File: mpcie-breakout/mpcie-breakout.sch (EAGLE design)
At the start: 34 parts, among them K1 694108106102, U1 IP4234CZ6, U2 LD1085D2T33R, X1 MPCIE-JAE, X2 MINI-USB-SHIELD-UX60-MB-5ST

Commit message: mpcie-breakout: Add Digikey LINK for all major parts
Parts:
- C1, C2, C4: CLASS (none) -> CAPACITOR; DESCRIPTION (none) -> NO DESCRIPTION; LINK (none) -> UNKNOWN LINK; MANUFACTURER (none) -> UNKNOWN MANUFACTURER; MANUFACTURERPARTNUMBER (none) -> UNKNOWN MANUFACTURER PART NUMBER; POPULATED (none) -> TRUE; ROHSCERTIFICATE (none) -> UNKNOWN ROHS CERTIFICATE; SOURCE (none) -> UNKNOWN SOURCE; SOURCEPARTNUMBER (none) -> UNKNOWN SOURCE PART NUMBER
- C3: CLASS (none) -> CAPACITOR; DESCRIPTION (none) -> NO DESCRIPTION; LINK (none) -> http://www.digikey.com/product-detail/en/nichicon/UUR0J471M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; MANUFACTURER (none) -> UNKNOWN MANUFACTURER; MANUFACTURERPARTNUMBER (none) -> UNKNOWN MANUFACTURER PART NUMBER; POPULATED (none) -> TRUE; ROHSCERTIFICATE (none) -> UNKNOWN ROHS CERTIFICATE; SOURCE (none) -> UNKNOWN SOURCE; SOURCEPARTNUMBER (none) -> UNKNOWN SOURCE PART NUMBER
- JP1, JP2, JP3, JP4: CLASS (none) -> CONNECTOR\JUMPER; DESCRIPTION (none) -> NO DESCRIPTION; LINK (none) -> UNKNOWN LINK; MANUFACTURER (none) -> UNKNOWN MANUFACTURER; MANUFACTURERPARTNUMBER (none) -> UNKNOWN MANUFACTURER PART NUMBER; POPULATED (none) -> TRUE; ROHSCERTIFICATE (none) -> UNKNOWN ROHS CERTIFICATE; SOURCE (none) -> UNKNOWN SOURCE; SOURCEPARTNUMBER (none) -> UNKNOWN SOURCE PART NUMBER
- K1: CLASS (none) -> RELAY; DESCRIPTION (none) -> NO DESCRIPTION; LINK (none) -> http://www.digikey.com/product-detail/en/wurth-electronics-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; MANUFACTURER (none) -> UNKNOWN MANUFACTURER; MANUFACTURERPARTNUMBER (none) -> UNKNOWN MANUFACTURER PART NUMBER; POPULATED (none) -> TRUE; ROHSCERTIFICATE (none) -> UNKNOWN ROHS CERTIFICATE; SOURCE (none) -> UNKNOWN SOURCE; SOURCEPARTNUMBER (none) -> UNKNOWN SOURCE PART NUMBER
- LED1, LED2: CLASS (none) -> LED; DESCRIPTION (none) -> NO DESCRIPTION; LINK (none) -> UNKNOWN LINK; MANUFACTURER (none) -> UNKNOWN MANUFACTURER; MANUFACTURERPARTNUMBER (none) -> UNKNOWN MANUFACTURER PART NUMBER; POPULATED (none) -> TRUE; ROHSCERTIFICATE (none) -> UNKNOWN ROHS CERTIFICATE; SOURCE (none) -> UNKNOWN SOURCE; SOURCEPARTNUMBER (none) -> UNKNOWN SOURCE PART NUMBER
- R1, R2, R3, R4, R5: CLASS (none) -> RESISTOR; DESCRIPTION (none) -> NO DESCRIPTION; LINK (none) -> UNKNOWN LINK; MANUFACTURER (none) -> UNKNOWN MANUFACTURER; MANUFACTURERPARTNUMBER (none) -> UNKNOWN MANUFACTURER PART NUMBER; POPULATED (none) -> TRUE; ROHSCERTIFICATE (none) -> UNKNOWN ROHS CERTIFICATE; SOURCE (none) -> UNKNOWN SOURCE; SOURCEPARTNUMBER (none) -> UNKNOWN SOURCE PART NUMBER
- SIM1: CLASS (none) -> UNKNOWN CLASS; DESCRIPTION (none) -> NO DESCRIPTION; LINK (none) -> http://www.digikey.com/product-detail/en/jae-electronics/SF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; MANUFACTURER (none) -> UNKNOWN MANUFACTURER; MANUFACTURERPARTNUMBER (none) -> UNKNOWN MANUFACTURER PART NUMBER; POPULATED (none) -> TRUE; ROHSCERTIFICATE (none) -> UNKNOWN ROHS CERTIFICATE; SOURCE (none) -> UNKNOWN SOURCE; SOURCEPARTNUMBER (none) -> UNKNOWN SOURCE PART NUMBER
- U1: CLASS (none) -> IC; DESCRIPTION (none) -> NO DESCRIPTION; LINK (none) -> http://www.digikey.com/product-detail/en/nxp-semiconductors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; MANUFACTURER (none) -> UNKNOWN MANUFACTURER; MANUFACTURERPARTNUMBER (none) -> UNKNOWN MANUFACTURER PART NUMBER; POPULATED (none) -> TRUE; ROHSCERTIFICATE (none) -> UNKNOWN ROHS CERTIFICATE; SOURCE (none) -> UNKNOWN SOURCE; SOURCEPARTNUMBER (none) -> UNKNOWN SOURCE PART NUMBER
- U2: CLASS (none) -> IC; DESCRIPTION (none) -> NO DESCRIPTION; LINK (none) -> http://www.digikey.com/product-detail/en/stmicroelectronics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; MANUFACTURER (none) -> UNKNOWN MANUFACTURER; MANUFACTURERPARTNUMBER (none) -> UNKNOWN MANUFACTURER PART NUMBER; POPULATED (none) -> TRUE; ROHSCERTIFICATE (none) -> UNKNOWN ROHS CERTIFICATE; SOURCE (none) -> UNKNOWN SOURCE; SOURCEPARTNUMBER (none) -> UNKNOWN SOURCE PART NUMBER
- X1: CLASS (none) -> CONNECTOR; DESCRIPTION (none) -> NO DESCRIPTION; LINK (none) -> https://www.digikey.de/product-detail/de/jae-electronics/MM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; MANUFACTURER (none) -> UNKNOWN MANUFACTURER; MANUFACTURERPARTNUMBER (none) -> UNKNOWN MANUFACTURER PART NUMBER; POPULATED (none) -> TRUE; ROHSCERTIFICATE (none) -> UNKNOWN ROHS CERTIFICATE; SOURCE (none) -> UNKNOWN SOURCE; SOURCEPARTNUMBER (none) -> UNKNOWN SOURCE PART NUMBER
- X2: CLASS (none) -> CONNECTOR; DESCRIPTION (none) -> NO DESCRIPTION; LINK (none) -> http://www.digikey.com/product-detail/en/hirose-electric-co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; MANUFACTURER (none) -> UNKNOWN MANUFACTURER; MANUFACTURERPARTNUMBER (none) -> UNKNOWN MANUFACTURER PART NUMBER; POPULATED (none) -> TRUE; ROHSCERTIFICATE (none) -> UNKNOWN ROHS CERTIFICATE; SOURCE (none) -> UNKNOWN SOURCE; SOURCEPARTNUMBER (none) -> UNKNOWN SOURCE PART NUMBER

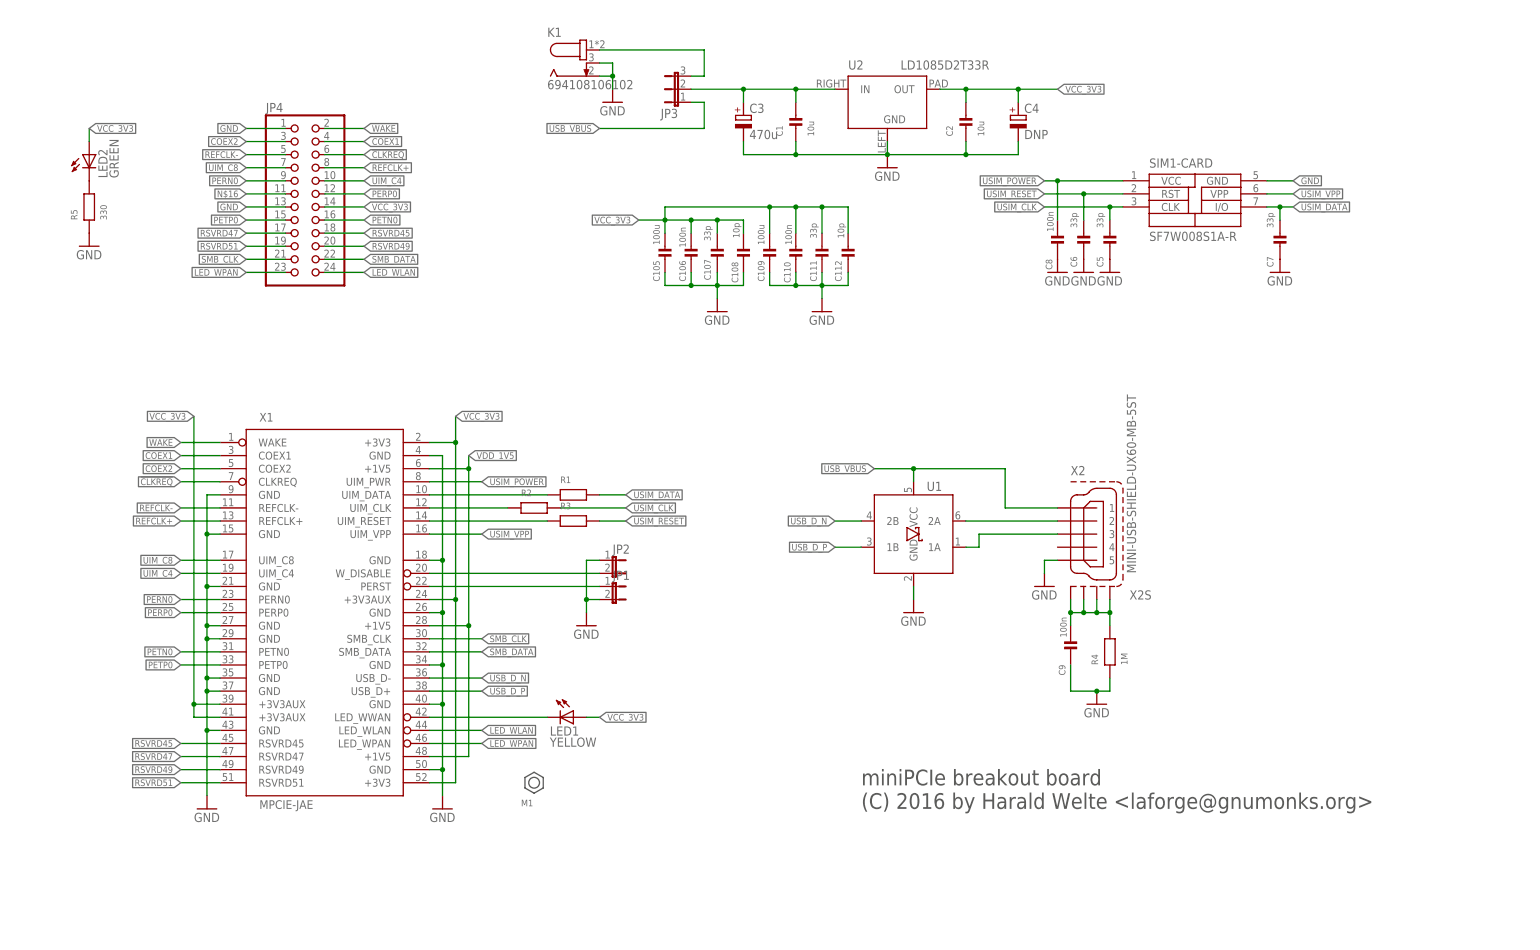
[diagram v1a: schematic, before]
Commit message: mpcie-breakout: Beautify schematics
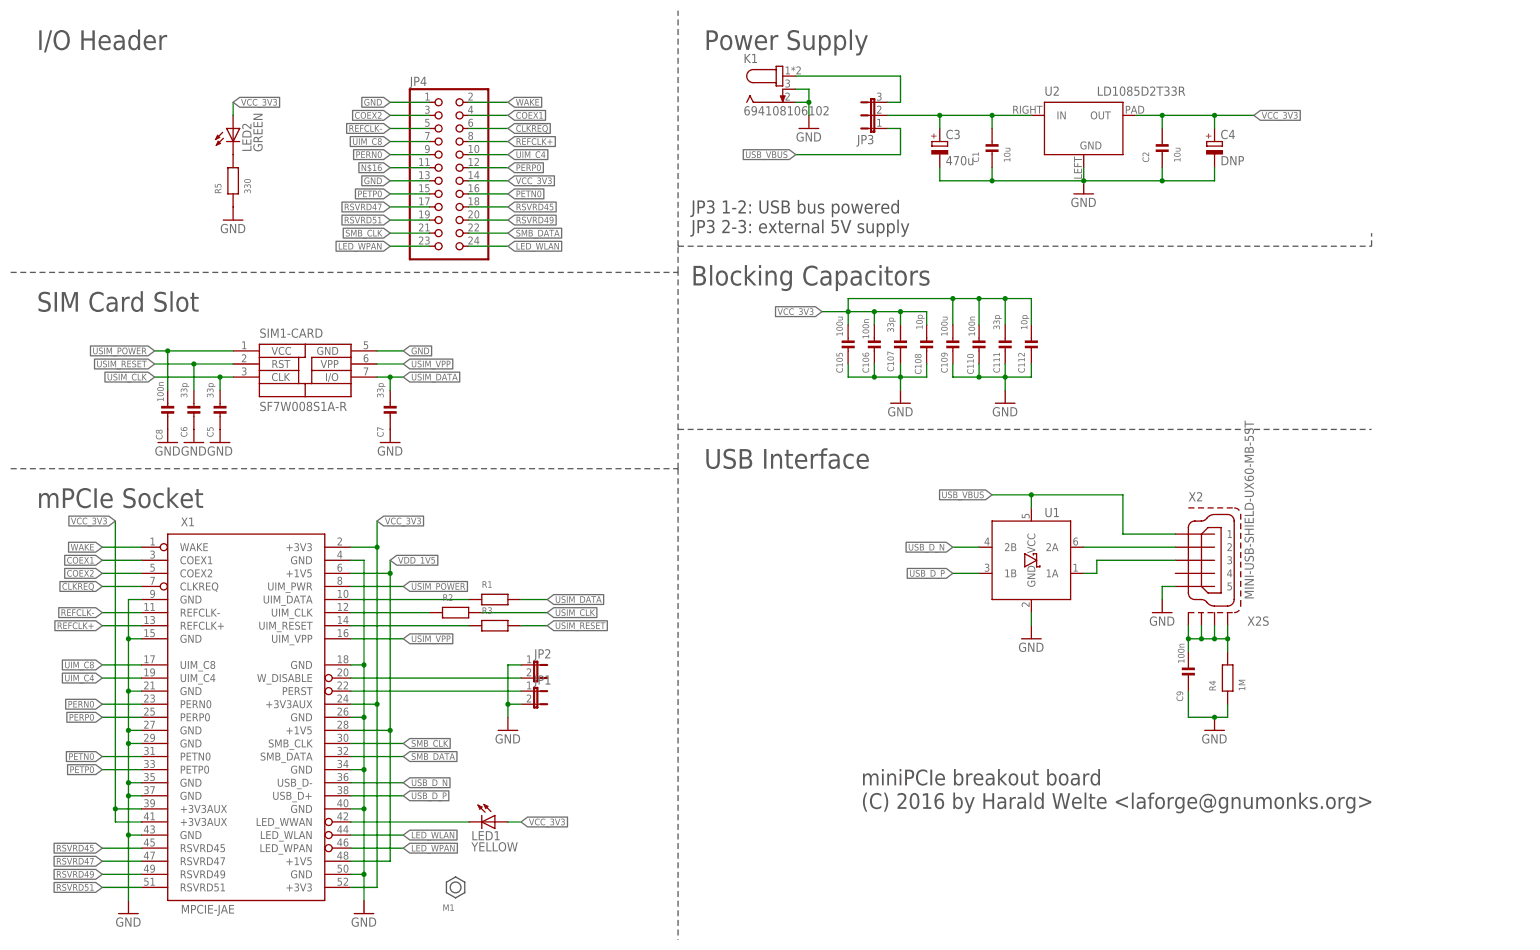
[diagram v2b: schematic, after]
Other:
- note added: "Blocking Capacitors"
- note added: "I/O Header"
- note added: "JP3 1-2: USB bus powered JP3 2-3: external 5V supply"
- note added: "Power Supply"
- note added: "SIM Card Slot"
- note added: "USB Interface"
- note added: "mPCIe Socket"
- moved on the sheet: C1, C105, C106, C107, C108, C109, C110, C111, C112, C2, C3, C4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

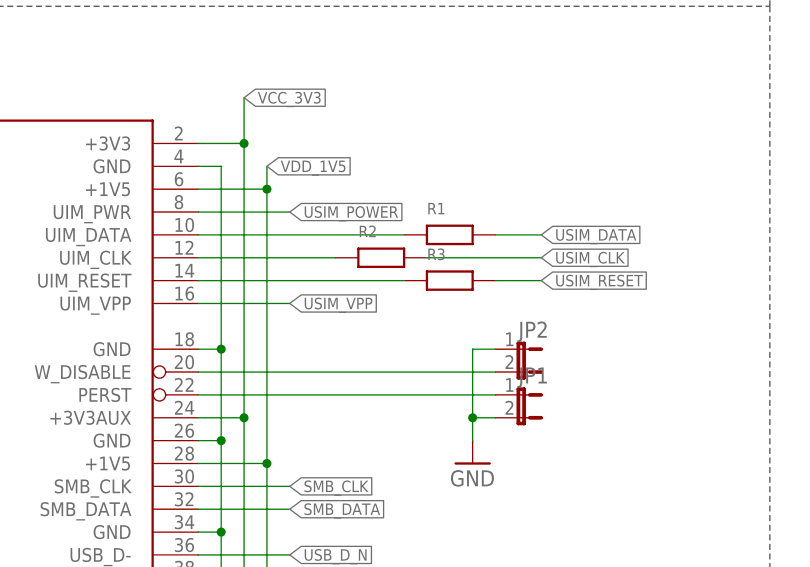
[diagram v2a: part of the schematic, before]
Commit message: mpci-breakout: Add BOM attributes + export BOM
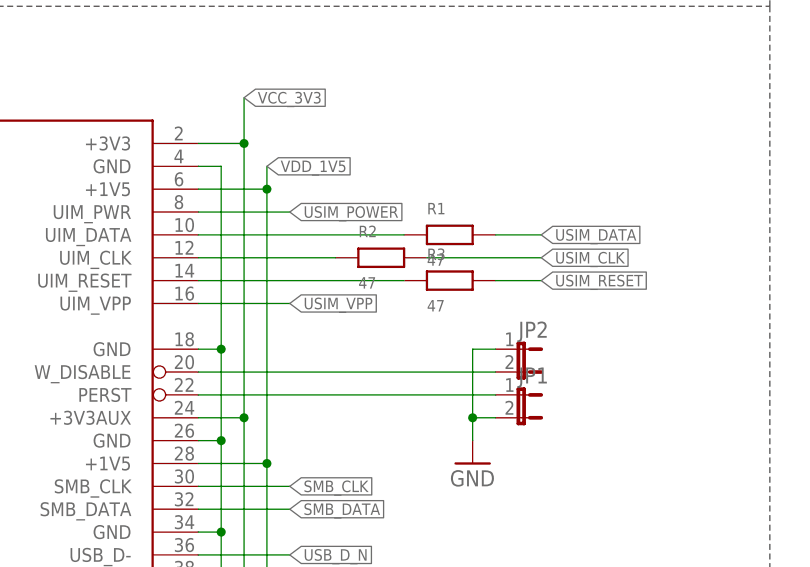
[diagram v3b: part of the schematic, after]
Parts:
- C1, C2: DESCRIPTION NO DESCRIPTION -> 10µF 16V Ceramic Capacitor X5R 0805 (2012 Metric) 0.079" L 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; LINK UNKNOWN LINK -> http://www.digikey.com/product-detail/en/samsung-electro-me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; MANUFACTURER UNKNOWN MANUFACTURER -> Samsung Electro-Mechanics America, Inc.; MANUFACTURERPARTNUMBER UNKNOWN MANUFACTURER PART NUMBER -> CL21A106KOQNNNG; SOURCE UNKNOWN SOURCE -> DIGIKEY; SOURCEPARTNUMBER UNKNOWN SOURCE PART NUMBER -> 1276-6455-1-ND
- C105, C109: LINK http://www.digikey.de/product-detail/de/CL32A107MQVNNNE/127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 -> http://www.digikey.com/product-detail/en/CL32A107MQVNNNE/12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
- C106, C110, C8, C9: LINK http://www.digikey.de/product-detail/de/foo/1276-1005-1-ND -> http://www.digikey.com/product-detail/en/foo/1276-1005-1-ND
- C107, C111, C5, C6, C7: LINK http://www.digikey.de/product-detail/de/CL05C330JB5NNNC/127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 -> http://www.digikey.com/product-detail/en/CL05C330JB5NNNC/12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
- C108, C112: LINK http://www.digikey.de/product-detail/de/C0603C100J5GACTU/39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 -> http://www.digikey.com/product-detail/en/C0603C100J5GACTU/3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
- C3: DESCRIPTION NO DESCRIPTION -> 470µF 6.3V Aluminum Capacitors Radial, Can - SMD 2000 Hrs @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; MANUFACTURER UNKNOWN MANUFACTURER -> Nichicon; MANUFACTURERPARTNUMBER UNKNOWN MANUFACTURER PART NUMBER -> UUR0J471MNL1GS; SOURCE UNKNOWN SOURCE -> DIGIKEY; SOURCEPARTNUMBER UNKNOWN SOURCE PART NUMBER -> 493-6207-1-ND
- JP4: DESCRIPTION NO DESCRIPTION -> 24 Positions Header, Unshrouded, Breakaway Connector 0.100"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; LINK UNKNOWN LINK -> http://www.digikey.com/product-detail/en/sullins-connector-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; MANUFACTURER UNKNOWN MANUFACTURER -> Sullins Connector Solutions; MANUFACTURERPARTNUMBER UNKNOWN MANUFACTURER PART NUMBER -> PRPC012DAAN-RC; SOURCE UNKNOWN SOURCE -> DIGIKEY; SOURCEPARTNUMBER UNKNOWN SOURCE PART NUMBER -> S2011EC-12-ND
- K1: DESCRIPTION NO DESCRIPTION -> Power Barrel Connector Jack 2.50mm ID (0.098"), 5.50mm OD (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; MANUFACTURER UNKNOWN MANUFACTURER -> Wurth Electronics Inc; MANUFACTURERPARTNUMBER UNKNOWN MANUFACTURER PART NUMBER -> 694108106102; SOURCE UNKNOWN SOURCE -> DIGIKEY; SOURCEPARTNUMBER UNKNOWN SOURCE PART NUMBER -> 732-5933-1-ND
- R1, R2, R3: value (none) -> 47; DESCRIPTION NO DESCRIPTION -> RES SMD 47 OHM 5% 1/10W 0603; LINK UNKNOWN LINK -> http://www.digikey.com/product-detail/en/yageo/RC0603JR-074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; MANUFACTURER UNKNOWN MANUFACTURER -> Yageo; MANUFACTURERPARTNUMBER UNKNOWN MANUFACTURER PART NUMBER -> RC0603JR-0747RL; SOURCE UNKNOWN SOURCE -> DIGIKEY; SOURCEPARTNUMBER UNKNOWN SOURCE PART NUMBER -> 311-47GRCT-ND
- R4: DESCRIPTION NO DESCRIPTION -> RES SMD 1M OHM 5% 1/20W 0201; LINK UNKNOWN LINK -> http://www.digikey.com/product-detail/en/samsung-electro-me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; MANUFACTURER UNKNOWN MANUFACTURER -> Samsung Electro-Mechanics America, Inc.; MANUFACTURERPARTNUMBER UNKNOWN MANUFACTURER PART NUMBER -> RC0603J105CS; SOURCE UNKNOWN SOURCE -> DIGIKEY; SOURCEPARTNUMBER UNKNOWN SOURCE PART NUMBER -> 1276-3856-1-ND
- R5: DESCRIPTION NO DESCRIPTION -> RES SMD 330 OHM 5% 1/10W 0603; LINK UNKNOWN LINK -> http://www.digikey.com/product-detail/en/yageo/RC0603JR-073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; MANUFACTURER UNKNOWN MANUFACTURER -> Yageo; MANUFACTURERPARTNUMBER UNKNOWN MANUFACTURER PART NUMBER -> RC0603JR-07330RL; SOURCE UNKNOWN SOURCE -> DIGIKEY; SOURCEPARTNUMBER UNKNOWN SOURCE PART NUMBER -> 311-330GRCT-ND
- SIM1: DESCRIPTION NO DESCRIPTION -> 8 (6 + 2) Position Card Connector SIM Card Surface Mount, R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; MANUFACTURER UNKNOWN MANUFACTURER -> JAE Electronics; MANUFACTURERPARTNUMBER UNKNOWN MANUFACTURER PART NUMBER -> SF7W008S1AE900; SOURCE UNKNOWN SOURCE -> DIGIKEY; SOURCEPARTNUMBER UNKNOWN SOURCE PART NUMBER -> 670-2337-1-ND
- U1: DESCRIPTION NO DESCRIPTION -> TVS DIODE 5.5VWM 6TSOP; MANUFACTURER UNKNOWN MANUFACTURER -> NXP Semiconductors; MANUFACTURERPARTNUMBER UNKNOWN MANUFACTURER PART NUMBER -> IP4234CZ6,125; SOURCE UNKNOWN SOURCE -> DIGIKEY; SOURCEPARTNUMBER UNKNOWN SOURCE PART NUMBER -> 568-5869-1-ND
- U2: DESCRIPTION NO DESCRIPTION -> Linear Voltage Regulator IC Positive Fixed 1 Output 3.3V 3A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; MANUFACTURER UNKNOWN MANUFACTURER -> STMicroelectronics; MANUFACTURERPARTNUMBER UNKNOWN MANUFACTURER PART NUMBER -> LD1085D2T33R; SOURCE UNKNOWN SOURCE -> DIGIKEY; SOURCEPARTNUMBER UNKNOWN SOURCE PART NUMBER -> 497-1222-1-ND
- X1: DESCRIPTION NO DESCRIPTION -> CONN MINI EXPRESS CARD 52POS SMD; LINK https://www.digikey.de/product-detail/de/jae-electronics/MM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 -> http://www.digikey.com/product-detail/en/jae-electronics/MM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; MANUFACTURER UNKNOWN MANUFACTURER -> JAE Electronics; MANUFACTURERPARTNUMBER UNKNOWN MANUFACTURER PART NUMBER -> MM60-52B1-E1-R650; SOURCE UNKNOWN SOURCE -> DIGIKEY; SOURCEPARTNUMBER UNKNOWN SOURCE PART NUMBER -> 670-2275-1-ND
- X2: DESCRIPTION NO DESCRIPTION -> USB - mini B USB 2.0 Receptacle Connector 5 Position Surfac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; MANUFACTURER UNKNOWN MANUFACTURER -> Hirose Electric Co Ltd; MANUFACTURERPARTNUMBER UNKNOWN MANUFACTURER PART NUMBER -> UX60-MB-5ST; SOURCE UNKNOWN SOURCE -> DIGIKEY; SOURCEPARTNUMBER UNKNOWN SOURCE PART NUMBER -> H2959CT-ND

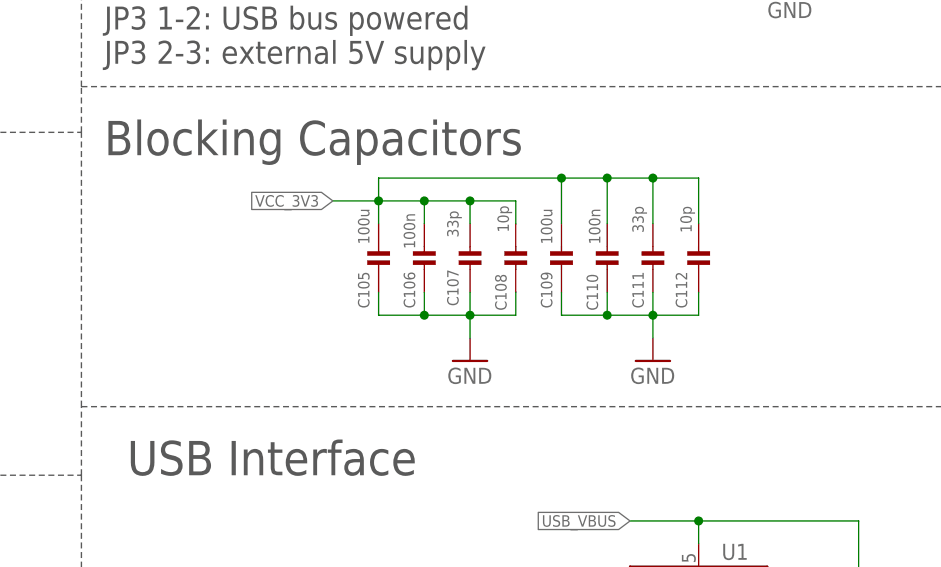
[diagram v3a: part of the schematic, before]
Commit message: mpcie-breakout: change 100uF caps from 1210 to 1206, reducing height
The current 100uF caps are too high at 2.9mm.  They touch the shielding
can of Quectel EC-20 modules, for exampel.  Let's use 1206 packaged
versions at 1.6mm instead.  Also, add two more, for safety.
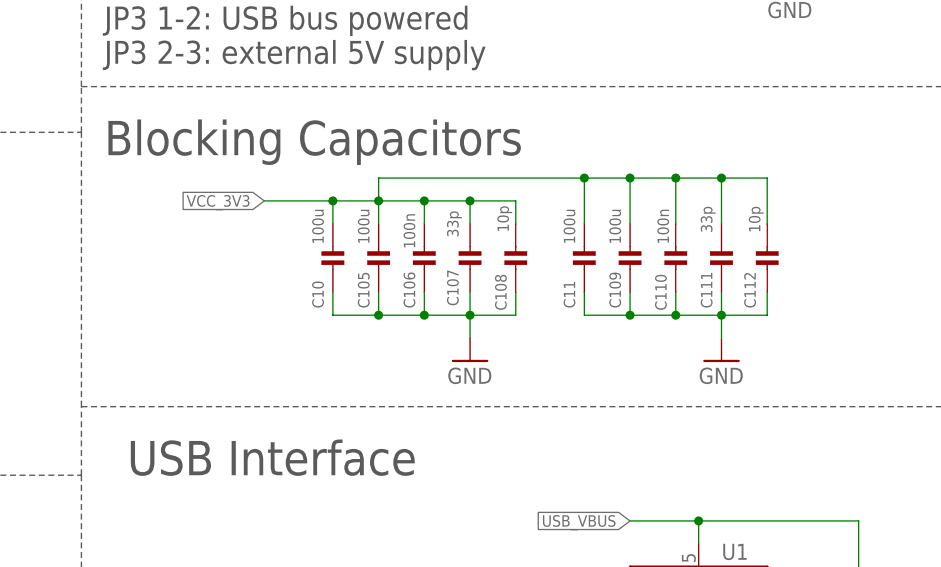
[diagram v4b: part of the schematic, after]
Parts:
- added C10, C11: 100u, rc-sysmocom:CAP_CERAMIC1206
- C105, C109: device rc-sysmocom:CAP_CERAMIC1210 -> rc-sysmocom:CAP_CERAMIC1206; DESCRIPTION CAP CER 100UF 6.3V X5R 1210 -> 100µF 6.3V Ceramic Capacitor X5R 1206 (3216 Metric) 0.126" 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; LINK http://www.digikey.com/product-detail/en/CL32A107MQVNNNE/12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 -> http://www.digikey.com/product-detail/en/murata-electronics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; MANUFACTURER Samsung Electro-Mechanics America, Inc. -> Murata Electronics North America; MANUFACTURERPARTNUMBER CL32A107MQVNNNE -> GRM31CR60J107ME39K; ROHSCERTIFICATE Bleifrei / RoHS-konform -> UNKNOWN ROHS CERTIFICATE; SOURCEPARTNUMBER 1276-1092-1-ND -> 490-7217-1-ND
- JP4: DESCRIPTION 24 Positions Header, Unshrouded, Breakaway Connector 0.100"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 -> 24 Positions Header, Unshrouded Connector 0.100" (2.54mm) T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; LINK http://www.digikey.com/product-detail/en/sullins-connector-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 -> http://www.digikey.com/product-detail/en/961224-6404-AR/3M9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; MANUFACTURER Sullins Connector Solutions -> 3M; MANUFACTURERPARTNUMBER PRPC012DAAN-RC -> 961224-6404-AR; SOURCEPARTNUMBER S2011EC-12-ND -> 3M9463-ND
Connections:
- net GND: now also C10.1, C11.1
- net VCC_3V3: now also C10.2, C11.2
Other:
- moved on the sheet: C109, C110, C111, C112
